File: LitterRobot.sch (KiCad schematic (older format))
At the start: 5 parts, among them J1 DF11C-4DP-2V(57), J2 DF11C-6DP-2V(57), J3 DF11C-8DP-2V(57), J4 DF11C-6DP-2V(57)

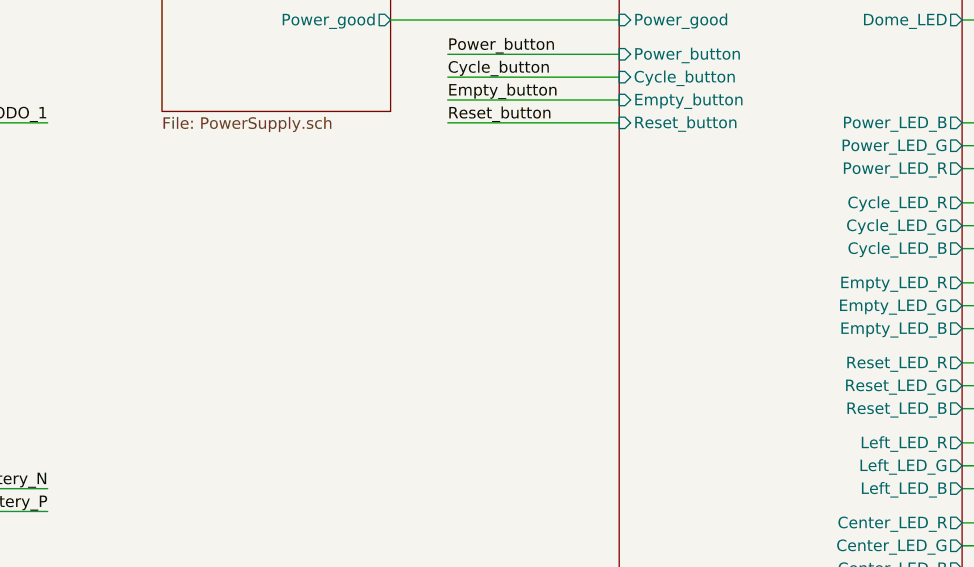
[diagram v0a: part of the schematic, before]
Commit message: Add an ambient light sensor
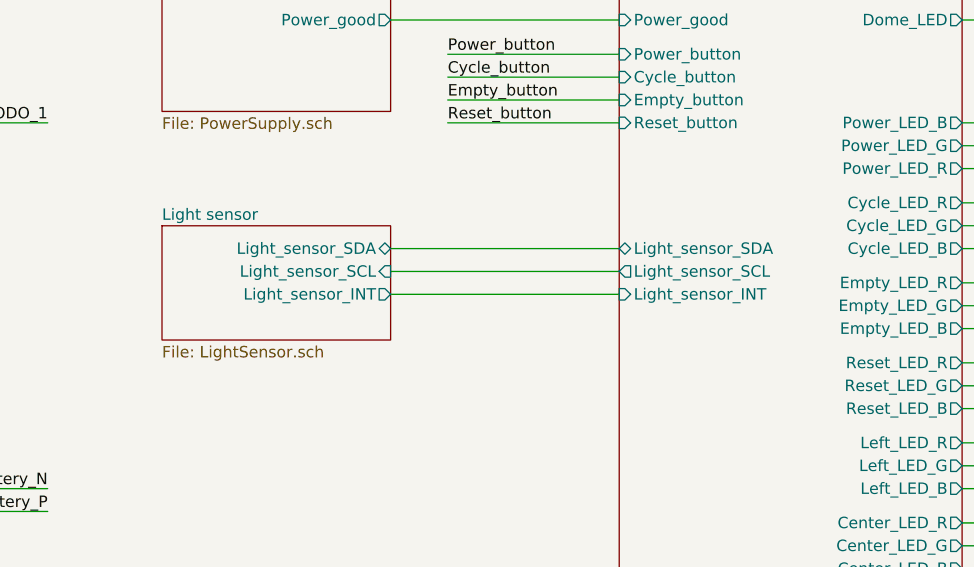
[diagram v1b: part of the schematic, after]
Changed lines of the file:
@@
 $Descr A4 11693 8268
 encoding utf-8
-Sheet 1 16
+Sheet 1 17
 Title "Litter Robot 3 - Main board"
 Date "2021-02-27"
@@
 F29 "Power_LED_R" O R 7500 1750 50
 F30 "Dome_LED" O R 7500 1100 50
+F31 "Light_sensor_SDA" B L 6000 2100 50
+F32 "Light_sensor_SCL" O L 6000 2200 50
+F33 "Light_sensor_INT" I L 6000 2300 50
 $EndSheet
 Wire Wire Line
@@
 Dome_LED_N
 $Comp
-L power:+15V #PWR?
+L power:+15V #PWR03
 U 1 1 60622B0D
 P 1650 5950
-F 0 "#PWR?" H 1650 5800 50  0001 C CNN
+F 0 "#PWR03" H 1650 5800 50  0001 C CNN
 F 1 "+15V" H 1665 6123 50  0000 C CNN
 F 2 "" H 1650 5950 50  0001 C CNN
@@
 	1    0    0    -1
 $EndComp
+$Sheet
+S 4000 2000 1000 500
+U 60624089
+F0 "Light sensor" 50
+F1 "LightSensor.sch" 50
+F2 "Light_sensor_SDA" B R 5000 2100 50
+F3 "Light_sensor_SCL" I R 5000 2200 50
+F4 "Light_sensor_INT" O R 5000 2300 50
+$EndSheet
+Wire Wire Line
+	5000 2100 6000 2100
+Wire Wire Line
+	6000 2200 5000 2200
+Wire Wire Line
+	5000 2300 6000 2300
 $EndSCHEMATC

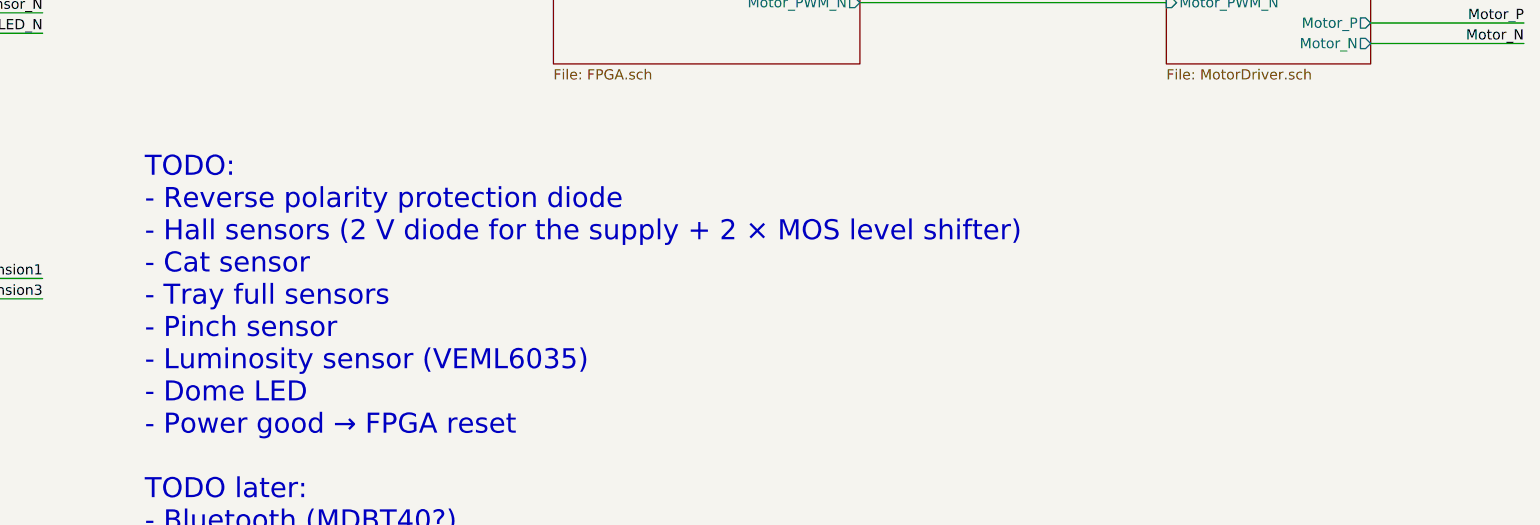
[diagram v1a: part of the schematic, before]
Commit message: Update the TODO lists
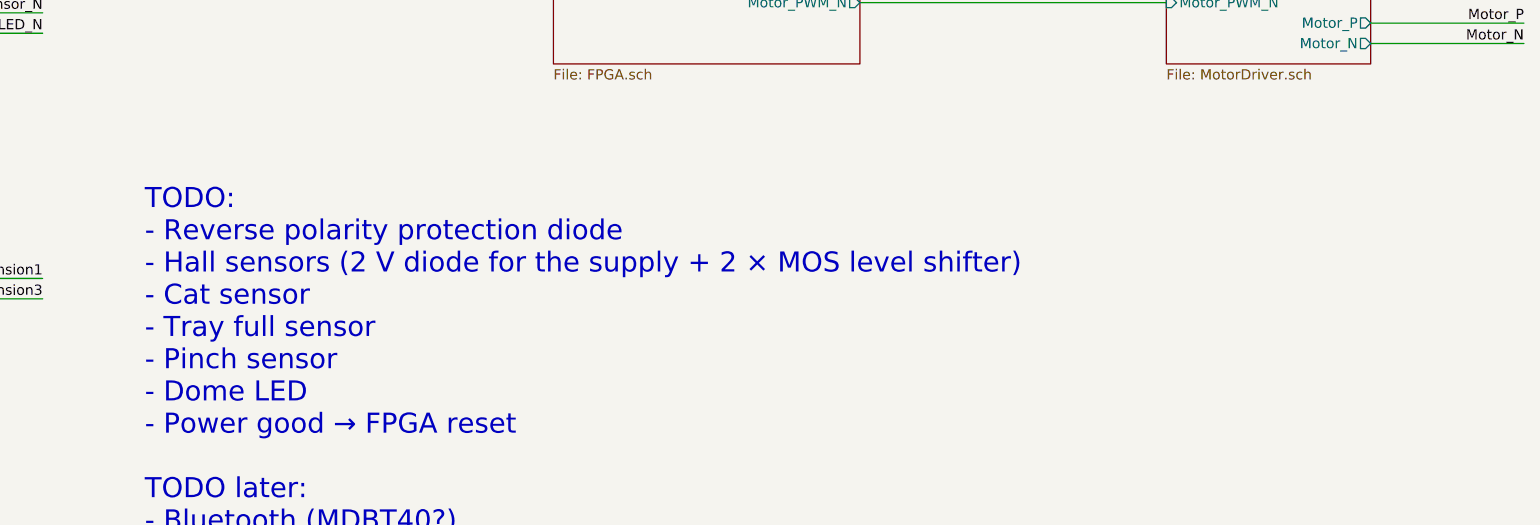
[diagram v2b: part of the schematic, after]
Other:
- note added: "TODO:\n- Reverse polarity protection diode\n- Hall sensors (2 V diode for the supply + 2 × MOS level shifter)\n- Cat sensor\n- Tray full sensor\n- Pinch sensor\n- Dome LED\n- Power good → FPGA reset\n\nTODO later:\n- Bluetooth (MDBT40?)"
- note removed: "TODO:\n- Reverse polarity protection diode\n- Hall sensors (2 V diode for the supply + 2 × MOS level shifter)\n- Cat sensor\n- Tray full sensors\n- Pinch sensor\n- Luminosity sensor (VEML6035)\n- Dome LED\n- Power good → FPGA reset\n\nTODO later:\n- Bluetooth (MDBT40?)"
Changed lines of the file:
@@
 	1250 3050 2000 3050
 Text Notes 4000 7300 0    98   ~ 0
-TODO:\n- Reverse polarity protection diode\n- Hall sensors (2 V diode for the supply + 2 × MOS level shifter)\n- Cat sensor\n- Tray full sensors\n- Pinch sensor\n- Luminosity sensor (VEML6035)\n- Dome LED\n- Power good → FPGA reset\n\nTODO later:\n- Bluetooth (MDBT40?)
+TODO:\n- Reverse polarity protection diode\n- Hall sensors (2 V diode for the supply + 2 × MOS level shifter)\n- Cat sensor\n- Tray full sensor\n- Pinch sensor\n- Dome LED\n- Power good → FPGA reset\n\nTODO later:\n- Bluetooth (MDBT40?)
 Text Label 1000 4850 0    50   ~ 0
 Dome_LED_P
